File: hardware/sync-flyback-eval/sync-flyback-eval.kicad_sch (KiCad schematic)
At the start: 97 parts, among them J1 RJ45_LED_Shielded, Q1 SiR422DP, Q2 Si7898DP, Q3 MMDT3906, T1 PoE_Transformer, T2 Pulse_Transformer, U1 TPS23754PWPR, U2 TCMT1107

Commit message: flyback: fix footprints for R3, R6, and D3
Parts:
- D3: footprint Diode_SMD:D_0402_1005Metric -> Diode_SMD:D_SMA
- R3, R6: footprint Resistor_SMD:R_0402_1005Metric -> Resistor_SMD:R_0805_2012Metric
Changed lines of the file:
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@@
       (effects (font (size 1.27 1.27)) (justify left) hide)
     )
-    (property "Footprint" "Diode_SMD:D_0402_1005Metric" (id 2) (at 25.4 53.34 0)
+    (property "Footprint" "Diode_SMD:D_SMA" (id 2) (at 25.4 53.34 0)
       (effects (font (size 1.27 1.27)) hide)
     )
@@
     (property "Reference" "R6" (id 0) (at 158.75 49.7078 90))
     (property "Value" "10" (id 1) (at 158.75 47.3964 90))
-    (property "Footprint" "Resistor_SMD:R_0402_1005Metric" (id 2) (at 158.75 46.228 90)
+    (property "Footprint" "Resistor_SMD:R_0805_2012Metric" (id 2) (at 158.75 46.228 90)
       (effects (font (size 1.27 1.27)) hide)
     )
@@
     (property "Reference" "R3" (id 0) (at 217.17 34.1122 90))
     (property "Value" "10" (id 1) (at 217.17 36.4236 90))
-    (property "Footprint" "Resistor_SMD:R_0402_1005Metric" (id 2) (at 217.17 37.592 90)
+    (property "Footprint" "Resistor_SMD:R_0805_2012Metric" (id 2) (at 217.17 37.592 90)
       (effects (font (size 1.27 1.27)) hide)
     )
@@
     )
     (path "/00000000-0000-0000-0000-00005c00f7a7"
-      (reference "D3") (unit 1) (value "D_Zener") (footprint "Diode_SMD:D_0402_1005Metric")
+      (reference "D3") (unit 1) (value "D_Zener") (footprint "Diode_SMD:D_SMA")
     )
     (path "/00000000-0000-0000-0000-00005be59e54"
@@
     )
     (path "/00000000-0000-0000-0000-00005d1f72be"
-      (reference "R3") (unit 1) (value "10") (footprint "Resistor_SMD:R_0402_1005Metric")
+      (reference "R3") (unit 1) (value "10") (footprint "Resistor_SMD:R_0805_2012Metric")
     )
     (path "/00000000-0000-0000-0000-00005e5b1c5f"
@@
     )
     (path "/00000000-0000-0000-0000-00005c2c2030"
-      (reference "R6") (unit 1) (value "10") (footprint "Resistor_SMD:R_0402_1005Metric")
+      (reference "R6") (unit 1) (value "10") (footprint "Resistor_SMD:R_0805_2012Metric")
     )
     (path "/4ede36d6-f7e9-4a55-b79f-e40a3ba5a33e"

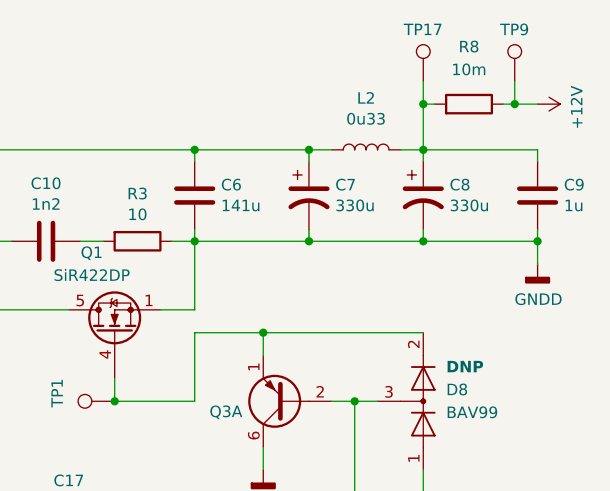
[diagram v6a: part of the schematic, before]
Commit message: flyback: fix value of C6 and add voltage designators to C6-C9
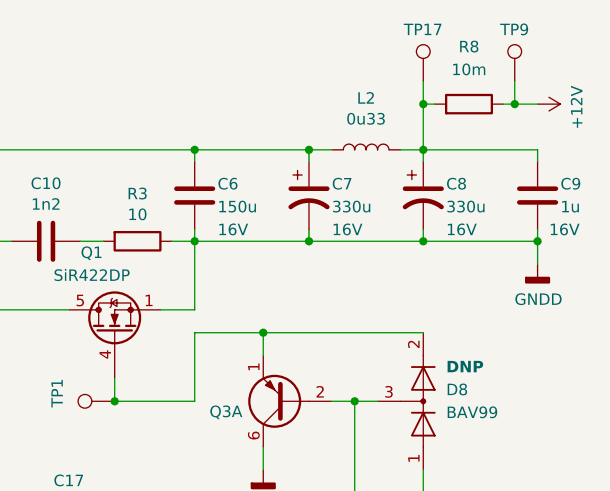
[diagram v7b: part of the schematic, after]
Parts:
- C6: value 141u -> 150u; Voltage (none) -> 16V
- C7, C8, C9: Voltage (none) -> 16V
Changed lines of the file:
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@@
   (symbol (lib_id "Device:C") (at 223.52 34.29 0) (unit 1)
     (in_bom yes) (on_board yes)
-    (property "Reference" "C6" (id 0) (at 226.441 33.1216 0)
-      (effects (font (size 1.27 1.27)) (justify left))
-    )
-    (property "Value" "141u" (id 1) (at 226.441 35.433 0)
+    (property "Reference" "C6" (id 0) (at 226.06 33.02 0)
+      (effects (font (size 1.27 1.27)) (justify left))
+    )
+    (property "Value" "150u" (id 1) (at 226.06 35.56 0)
       (effects (font (size 1.27 1.27)) (justify left))
     )
@@
       (effects (font (size 1.27 1.27)) hide)
     )
+    (property "Voltage" "16V" (id 4) (at 226.06 38.1 0)
+      (effects (font (size 1.27 1.27)) (justify left))
+    )
     (pin "1")
     (pin "2")
@@
   (symbol (lib_id "Device:C_Polarized_US") (at 236.22 34.29 0) (unit 1)
     (in_bom yes) (on_board yes)
-    (property "Reference" "C7" (id 0) (at 239.141 33.1216 0)
-      (effects (font (size 1.27 1.27)) (justify left))
-    )
-    (property "Value" "330u" (id 1) (at 239.141 35.433 0)
+    (property "Reference" "C7" (id 0) (at 238.76 33.02 0)
+      (effects (font (size 1.27 1.27)) (justify left))
+    )
+    (property "Value" "330u" (id 1) (at 238.76 35.56 0)
       (effects (font (size 1.27 1.27)) (justify left))
     )
@@
       (effects (font (size 1.27 1.27)) hide)
     )
+    (property "Voltage" "16V" (id 4) (at 238.76 38.1 0)
+      (effects (font (size 1.27 1.27)) (justify left))
+    )
     (pin "1")
     (pin "2")
@@
   (symbol (lib_id "Device:C_Polarized_US") (at 248.92 34.29 0) (unit 1)
     (in_bom yes) (on_board yes)
-    (property "Reference" "C8" (id 0) (at 251.841 33.1216 0)
-      (effects (font (size 1.27 1.27)) (justify left))
-    )
-    (property "Value" "330u" (id 1) (at 251.841 35.433 0)
+    (property "Reference" "C8" (id 0) (at 251.46 33.02 0)
+      (effects (font (size 1.27 1.27)) (justify left))
+    )
+    (property "Value" "330u" (id 1) (at 251.46 35.56 0)
       (effects (font (size 1.27 1.27)) (justify left))
     )
@@
       (effects (font (size 1.27 1.27)) hide)
     )
+    (property "Voltage" "16V" (id 4) (at 251.46 38.1 0)
+      (effects (font (size 1.27 1.27)) (justify left))
+    )
     (pin "1")
     (pin "2")
@@
   (symbol (lib_id "Device:C") (at 261.62 34.29 0) (unit 1)
     (in_bom yes) (on_board yes)
-    (property "Reference" "C9" (id 0) (at 264.541 33.1216 0)
-      (effects (font (size 1.27 1.27)) (justify left))
-    )
-    (property "Value" "1u" (id 1) (at 264.541 35.433 0)
+    (property "Reference" "C9" (id 0) (at 264.16 33.02 0)
+      (effects (font (size 1.27 1.27)) (justify left))
+    )
+    (property "Value" "1u" (id 1) (at 264.16 35.56 0)
       (effects (font (size 1.27 1.27)) (justify left))
     )
@@
     (property "Datasheet" "~" (id 3) (at 261.62 34.29 0)
       (effects (font (size 1.27 1.27)) hide)
+    )
+    (property "Voltage" "16V" (id 4) (at 262.89 38.1 0)
+      (effects (font (size 1.27 1.27)) (justify left))
     )
     (pin "1")
@@
     )
     (path "/00000000-0000-0000-0000-00005d269bfc"
-      (reference "C6") (unit 1) (value "141u") (footprint "Capacitor_SMD:C_Elec_6.3x7.7")
+      (reference "C6") (unit 1) (value "150u") (footprint "Capacitor_SMD:C_Elec_6.3x7.7")
     )
     (path "/00000000-0000-0000-0000-00005d2f3e39"
